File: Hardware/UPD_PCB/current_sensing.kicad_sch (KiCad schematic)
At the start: 48 parts, among them Q6 BSS84, U1 INA228, U2 INA228, U3 INA228, U4 INA228, U5 ACS711xEXLT-31AB

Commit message: Updated schematic
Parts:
- added TP5, TP6: TestPoint, TestPoint:TestPoint_Loop_D2.54mm_Drill1.5mm_Beaded, symbol Connector:TestPoint
- C23, C24, C27, C28: value C -> 100nF; footprint (none) -> Capacitor_SMD:C_0603_1608Metric_Pad1.08x0.95mm_HandSolder
- TP1, TP2, TP3, TP4: footprint (none) -> TestPoint:TestPoint_Loop_D2.54mm_Drill1.5mm_Beaded
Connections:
- net +5V: now also U2.1 (A1), U3.2 (A0), U4.1 (A1), U4.2 (A0)
- net GND: now also TP5.1, TP6.1; no longer U2.1 (A1), U3.2 (A0), U4.1 (A1), U4.2 (A0)

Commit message: Updated design
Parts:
- added C31: 0.1µF, symbol Device:C
- added C32: 100nF, Capacitor_SMD:C_0603_1608Metric_Pad1.08x0.95mm_HandSolder, symbol Device:C
- added R44: R_Shunt, symbol Device:R_Shunt
- added R45, R46: R50, Resistor_SMD:R_0603_1608Metric_Pad0.98x0.95mm_HandSolder, symbol Device:R
- added R47, R48, R49: 10k, Resistor_SMD:R_0603_1608Metric_Pad0.98x0.95mm_HandSolder, symbol Device:R
- added TP7: TestPoint, TestPoint:TestPoint_Loop_D2.54mm_Drill1.5mm_Beaded, symbol Connector:TestPoint
- added U6: INA228, Package_SO:VSSOP-10_3x3mm_P0.5mm, symbol Sensor_Energy:INA228
- C21, C22, C25, C26: value C -> 0.1µF
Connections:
- net +19V: no longer R24.1, TP4.1, U4.8 (Vbus)
- net +19V_out: no longer R24.4
- net +24V: no longer R12.1, TP2.1, U2.8 (Vbus)
- net +24V_out: no longer R12.4
- net +5V: now also R24.1, TP4.1, U4.8 (Vbus), C32.1, R47.2, R48.2, R49.2, U6.6 (VS)
- net GND: now also C32.2, U6.7 (GND)
- net INA_SCL: now also R48.1, U6.5 (SCL)
- net INA_SDA: now also R47.1, U6.1 (A1), U6.2 (A0), U6.4 (SDA)
- net INA_alert_19V: now also R49.1, U6.3 (~{Alert})
- new net: R44.2, R45.1
- new net: R44.3, R46.1
- new net: C31.1, R45.2, U6.10 (Vin+)
- new net: C31.2, R46.2, U6.9 (Vin-)
- new net +12V: R12.1, TP2.1, U2.8 (Vbus)
- new net +12V_out: R12.4
- new net +16V: R44.1, TP7.1, U6.8 (Vbus)
- new net +16V_out: R44.4
- new net +5V_out: R24.4
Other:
- moved on the sheet: C29, C30, D1, Q6, R31, R32, R33, R34, R35, R36, R37, U5

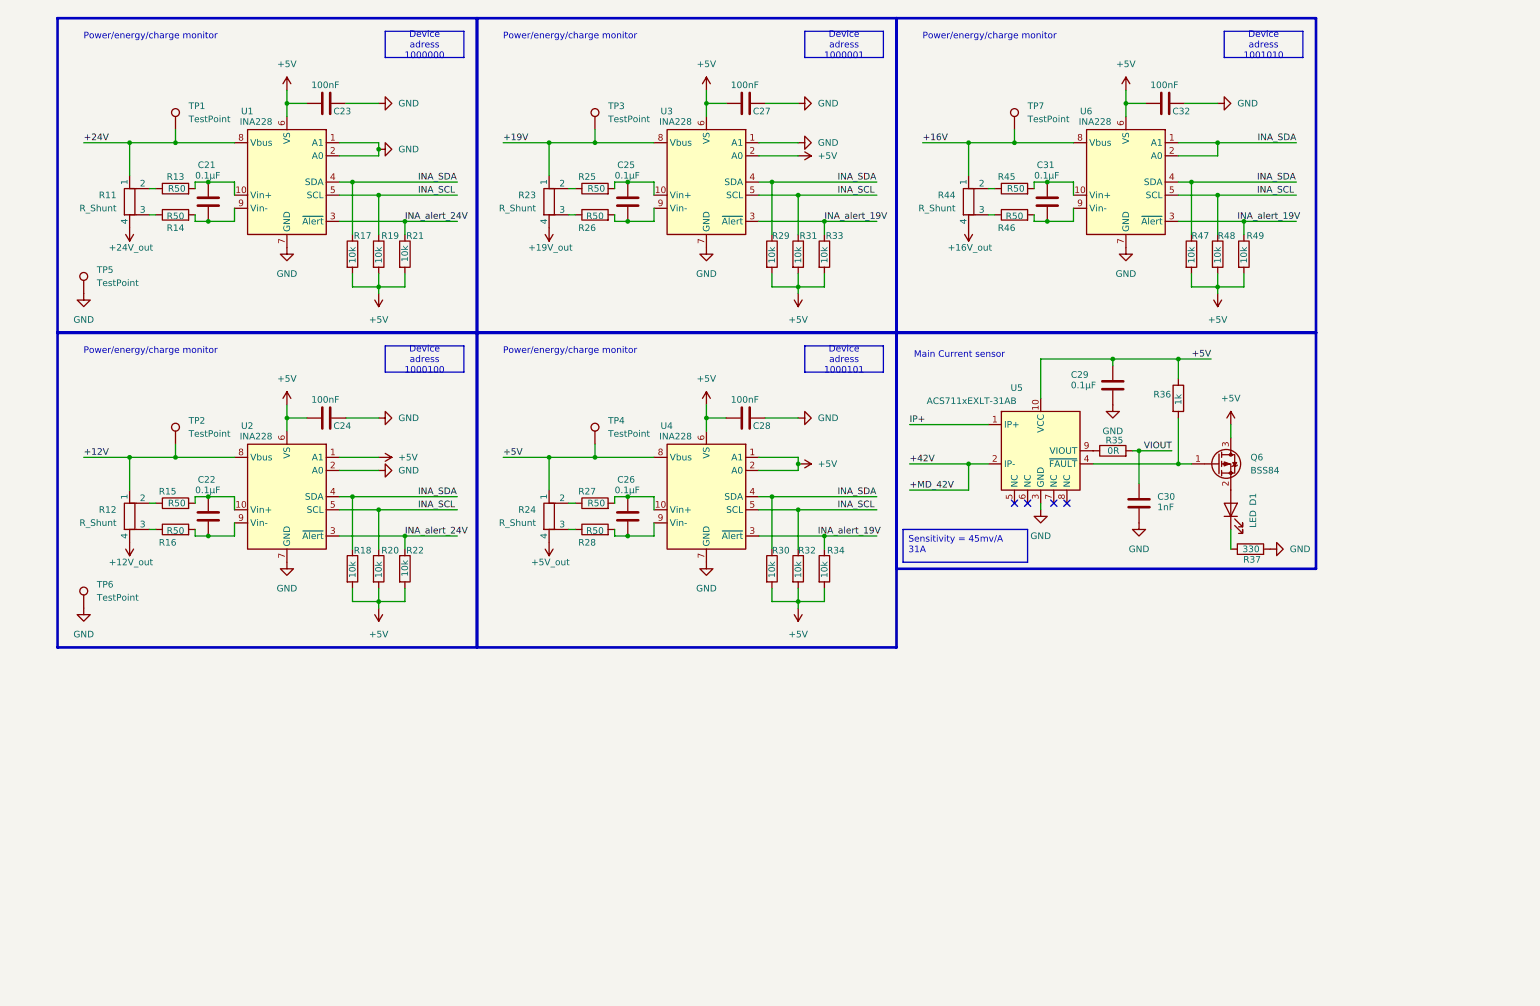
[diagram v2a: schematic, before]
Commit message: Updated schematic (before INA219 integration)
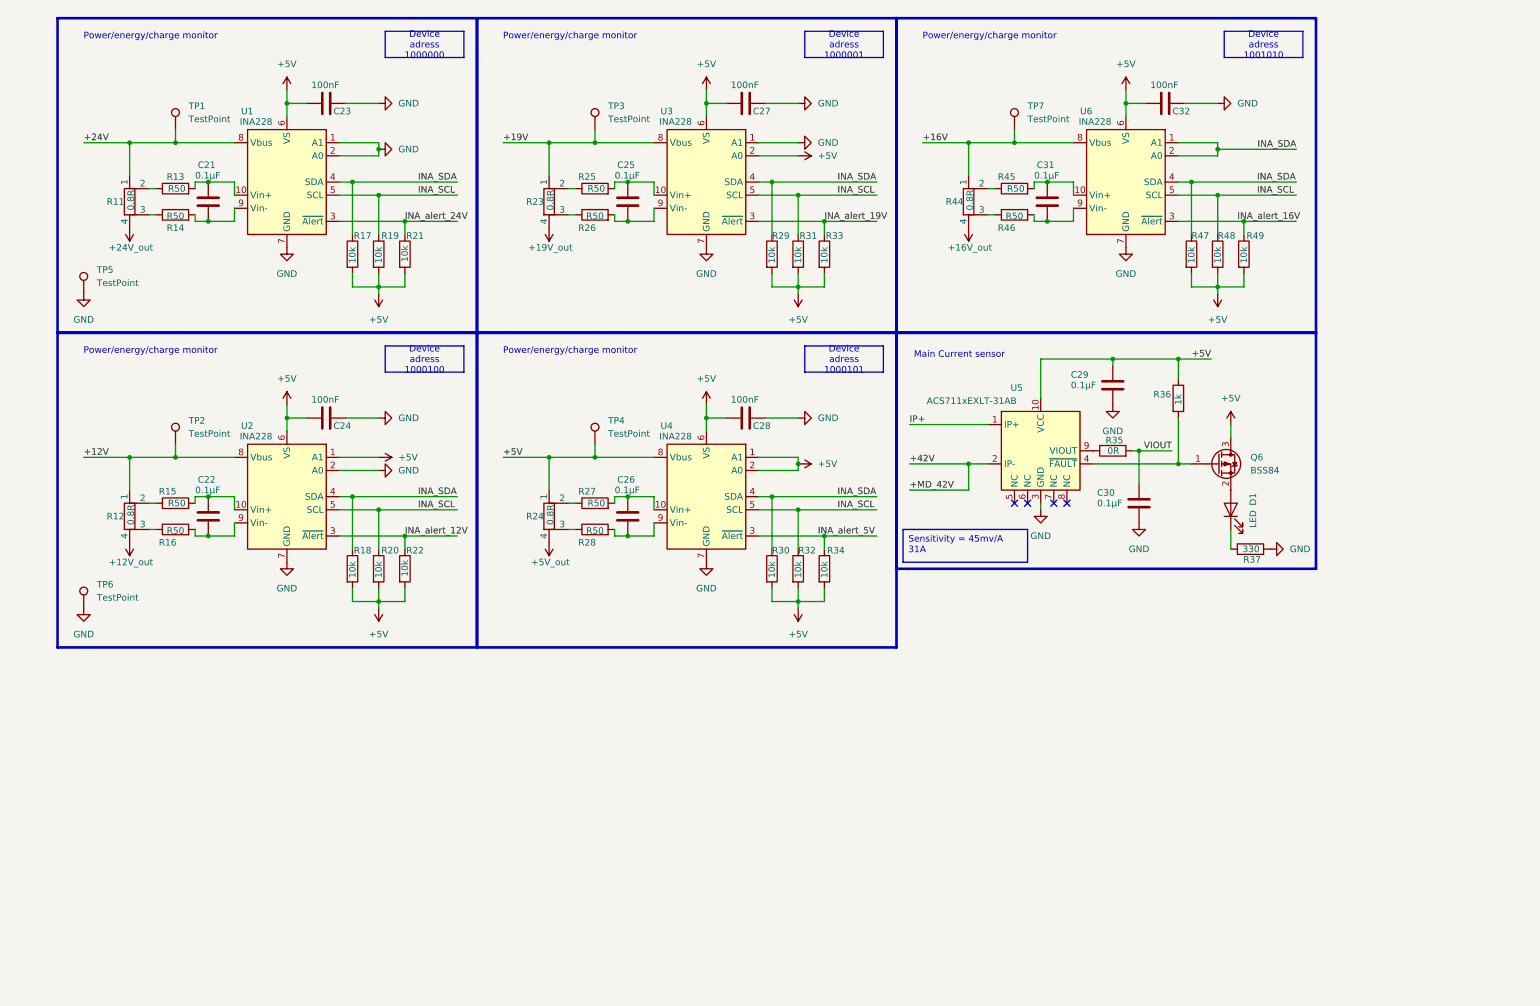
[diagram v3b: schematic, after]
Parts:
- C29: footprint (none) -> Capacitor_SMD:C_0603_1608Metric_Pad1.08x0.95mm_HandSolder
- C30: value 1nF -> 0.1µF; footprint (none) -> Capacitor_SMD:C_0603_1608Metric_Pad1.08x0.95mm_HandSolder
- D1: footprint (none) -> LED_SMD:LED_0603_1608Metric_Pad1.05x0.95mm_HandSolder
- R11, R12, R23, R24, R44: value R_Shunt -> 0.8R; footprint (none) -> Resistor_SMD:R_2512_6332Metric_Pad1.40x3.35mm_HandSolder
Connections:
- net INA_alert_19V: no longer R34.1, R49.1, U4.3 (~{Alert}), U6.3 (~{Alert})
- net INA_alert_24V: no longer R22.1, U2.3 (~{Alert})
- new net INA_alert_12V: R22.1, U2.3 (~{Alert})
- new net INA_alert_16V: R49.1, U6.3 (~{Alert})
- new net INA_alert_5V: R34.1, U4.3 (~{Alert})

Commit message: Finalized Schematic
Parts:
- removed C21, C22, C25, C26, C31: 0.1µF, symbol Device:C
- removed C23, C24, C27: 100nF, Capacitor_SMD:C_0603_1608Metric_Pad1.08x0.95mm_HandSolder, symbol Device:C
- removed R11, R12, R23, R24, R44: 0.8R, Resistor_SMD:R_2512_6332Metric_Pad1.40x3.35mm_HandSolder, symbol Device:R_Shunt
- removed R13, R14, R26, R27, R46: R50, Resistor_SMD:R_0603_1608Metric_Pad0.98x0.95mm_HandSolder, symbol Device:R
- removed R19, R20, R47, R48, R49: 10k, Resistor_SMD:R_0603_1608Metric_Pad0.98x0.95mm_HandSolder, symbol Device:R
- removed TP1, TP2: TestPoint, TestPoint:TestPoint_Loop_D2.54mm_Drill1.5mm_Beaded, symbol Connector:TestPoint
- removed U1, U2, U3, U4, U6: INA228, Package_SO:VSSOP-10_3x3mm_P0.5mm, symbol Sensor_Energy:INA228
- added C29, C33, C34, C35, C36, C37, C38, C39, C40, C41: 0.1µF, Capacitor_SMD:C_0603_1608Metric_Pad1.08x0.95mm_HandSolder, symbol Device:C
- added R13, R14, R26, R27, R36, R37: 0.2R, Resistor_SMD:R_Shunt_Vishay_WSK2512_6332Metric_T2.21mm, symbol Device:R_Shunt
- added R24, R35, R42, R43, R44: 10k, Resistor_SMD:R_0603_1608Metric_Pad0.98x0.95mm_HandSolder, symbol Device:R
- added R38, R39, R40, R41: R50, Resistor_SMD:R_0603_1608Metric_Pad0.98x0.95mm_HandSolder, symbol Device:R
- added TP5, TP6, TP8, TP9: TestPoint, TestPoint:TestPoint_Loop_D2.54mm_Drill1.5mm_Beaded, symbol Connector:TestPoint
- added U2, U3, U4, U5, U6, U7: INA219AxD, Package_SO:SOIC-8_3.9x4.9mm_P1.27mm, symbol Sensor_Energy:INA219AxD
- C28, C32: value 100nF -> 0.1µF
- R17, R18, R29, R30, R31: value 10k -> R50
- R25, R45: value R50 -> 10k
- renumbered C29 to C30, C30 to C31, Q6 to Q7, R35 to R19, R36 to R20, R37 to R23, TP5 to TP1, TP6 to TP2, U5 to U1
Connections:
- net INA_alert_12V is gone; now on net INA_SDA: R22.1
- net INA_alert_19V is gone; now on net INA_SDA: R33.1
- net INA_alert_24V is gone; now on net INA_SDA: R21.1
- net INA_alert_5V is gone; now on net INA_SCL: R34.1
- net +16V: now also R37.1, TP9.1; no longer TP7.1
- net +16V_out: now also R37.4
- net +19V: now also R26.1, TP6.1; no longer TP3.1
- net +19V_out: now also R26.4
- net +24V: now also TP3.1, R13.1
- net +24V_out: now also R13.4
- net +5V: now also C32.2, R25.2, R45.2, C33.2, C36.2, C37.2, C40.2, C41.2, R24.2, R35.2, R36.4, R42.2, R43.2, R44.2, U2.5 (VS), U3.1 (A1), U3.5 (VS), U4.2 (A0), U4.5 (VS), U5.5 (VS), U6.1 (A1), U6.2 (A0), U6.5 (VS), U7.5 (VS); no longer C28.1, C32.1, R17.2, R18.2, R29.2, R30.2, R31.2, TP4.1
- net GND: now also C32.1, C33.1, C36.1, C37.1, C40.1, C41.1, TP5.1, U2.1 (A1), U2.2 (A0), U2.6 (GND), U3.2 (A0), U3.6 (GND), U4.1 (A1), U4.6 (GND), U5.6 (GND), U6.6 (GND), U7.6 (GND); no longer C28.2, C32.2
- net INA_SCL: now also R25.1, R45.1, R24.1, R35.1, R44.1, U2.4 (SCL), U3.4 (SCL), U4.4 (SCL), U5.1 (A1), U5.2 (A0), U5.4 (SCL), U6.4 (SCL), U7.4 (SCL); no longer R31.1, R32.1
- net INA_SDA: now also R32.1, R42.1, R43.1, U2.3 (SDA), U3.3 (SDA), U4.3 (SDA), U5.3 (SDA), U6.3 (SDA), U7.1 (A1), U7.2 (A0), U7.3 (SDA); no longer R17.1, R18.1, R29.1, R30.1
- net at R28.1: now also R26.2
- net at R28.2: now also C34.1, U4.8 (IN+)
- net at R15.1: now also R13.2
- net at R15.2: now also C28.1, U2.8 (IN+)
- net at R16.2: now also C28.2, U2.7 (IN-)
- net at R16.1: now also R13.3
- new net: C39.1, R40.2, U7.8 (IN+)
- new net: C39.2, R41.2, U7.7 (IN-)
- new net: C38.2, R39.2, U6.7 (IN-)
- new net: C38.1, R38.2, U6.8 (IN+)
- new net: R27.2, R30.1
- new net: R27.3, R31.1
- new net: R26.3, R29.1
- new net: C34.2, R29.2, U4.7 (IN-)
- new net: C35.1, R30.2, U5.8 (IN+)
- new net: R36.2, R38.1
- new net: R37.3, R41.1
- new net: C35.2, R31.2, U5.7 (IN-)
- new net: R37.2, R40.1
- new net: R14.2, R17.1
- new net: R14.3, R18.1
- new net: C29.1, R17.2, U3.8 (IN+)
- new net: R36.3, R39.1
- new net: C29.2, R18.2, U3.7 (IN-)
- new net +12V_1: R14.1, TP4.1
- new net +12V_1_out: R14.4
- new net +12V_2: R27.1, TP7.1
- new net +12V_2_out: R27.4
- new net +5V_NS: R36.1, TP8.1
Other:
- moved on the sheet: C30, C31, D1, Q7, R19, R20, R23, TP1, TP2, U1

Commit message: First board layout
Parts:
- R13, R14, R26, R27, R36, R37: footprint Resistor_SMD:R_Shunt_Vishay_WSK2512_6332Metric_T2.21mm -> Library:R_shunt_different_pad_layout
- TP1, TP2, TP3, TP4, TP5, TP6, TP7, TP8, TP9: footprint TestPoint:TestPoint_Loop_D2.54mm_Drill1.5mm_Beaded -> TestPoint:TestPoint_THTPad_D1.0mm_Drill0.5mm

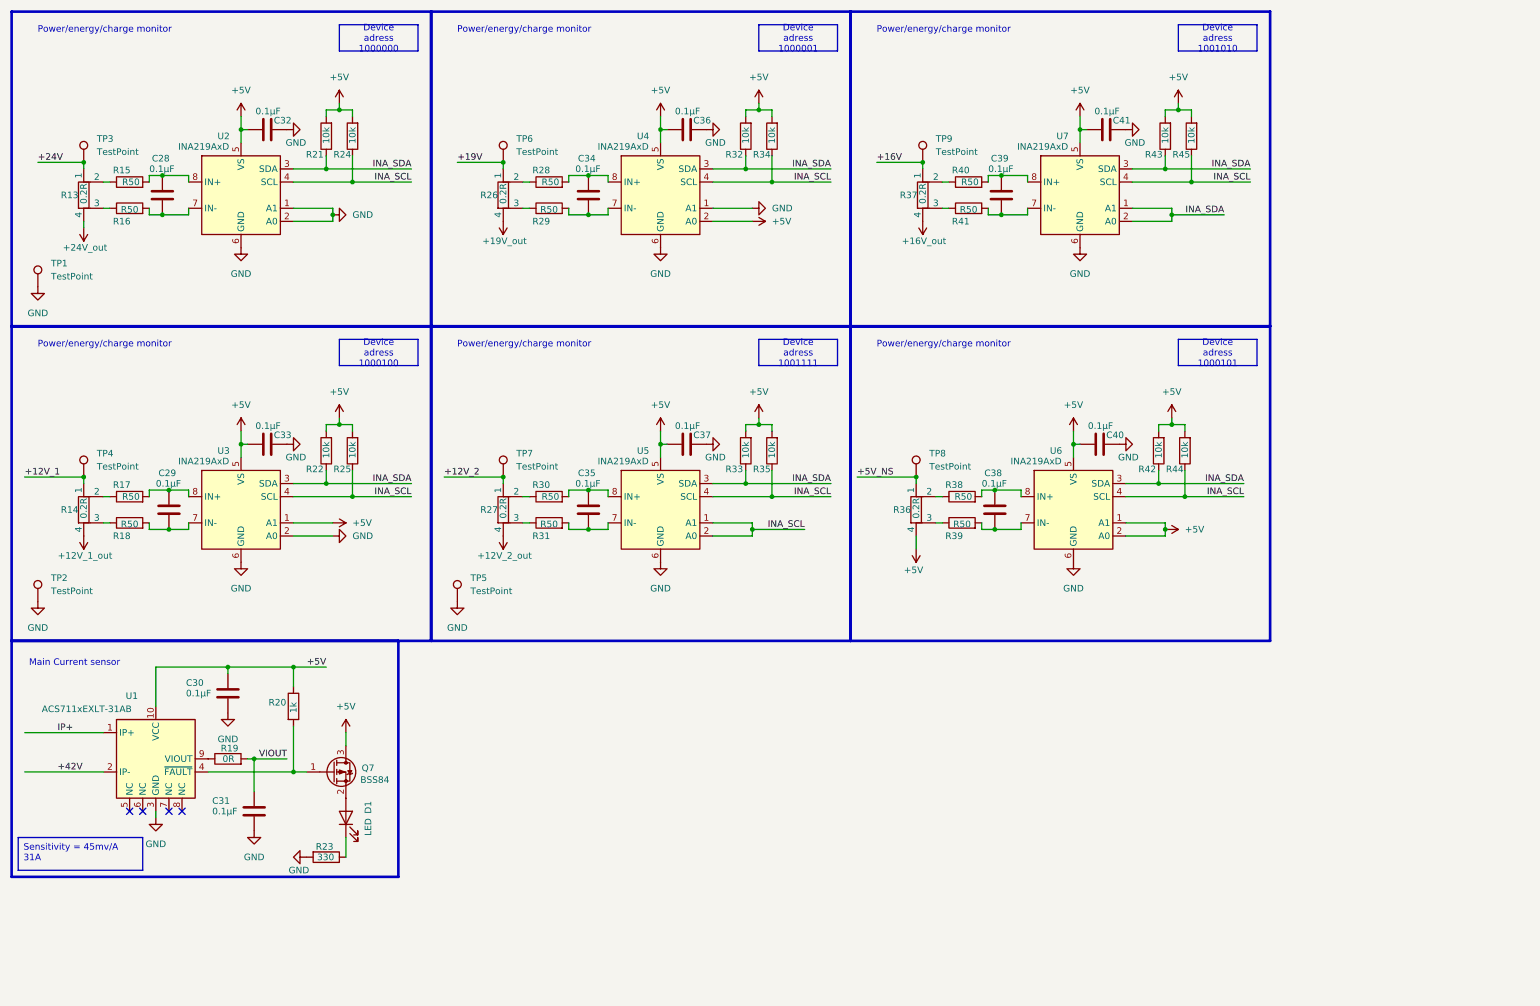
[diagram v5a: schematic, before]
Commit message: Pcb layout before changing inductor
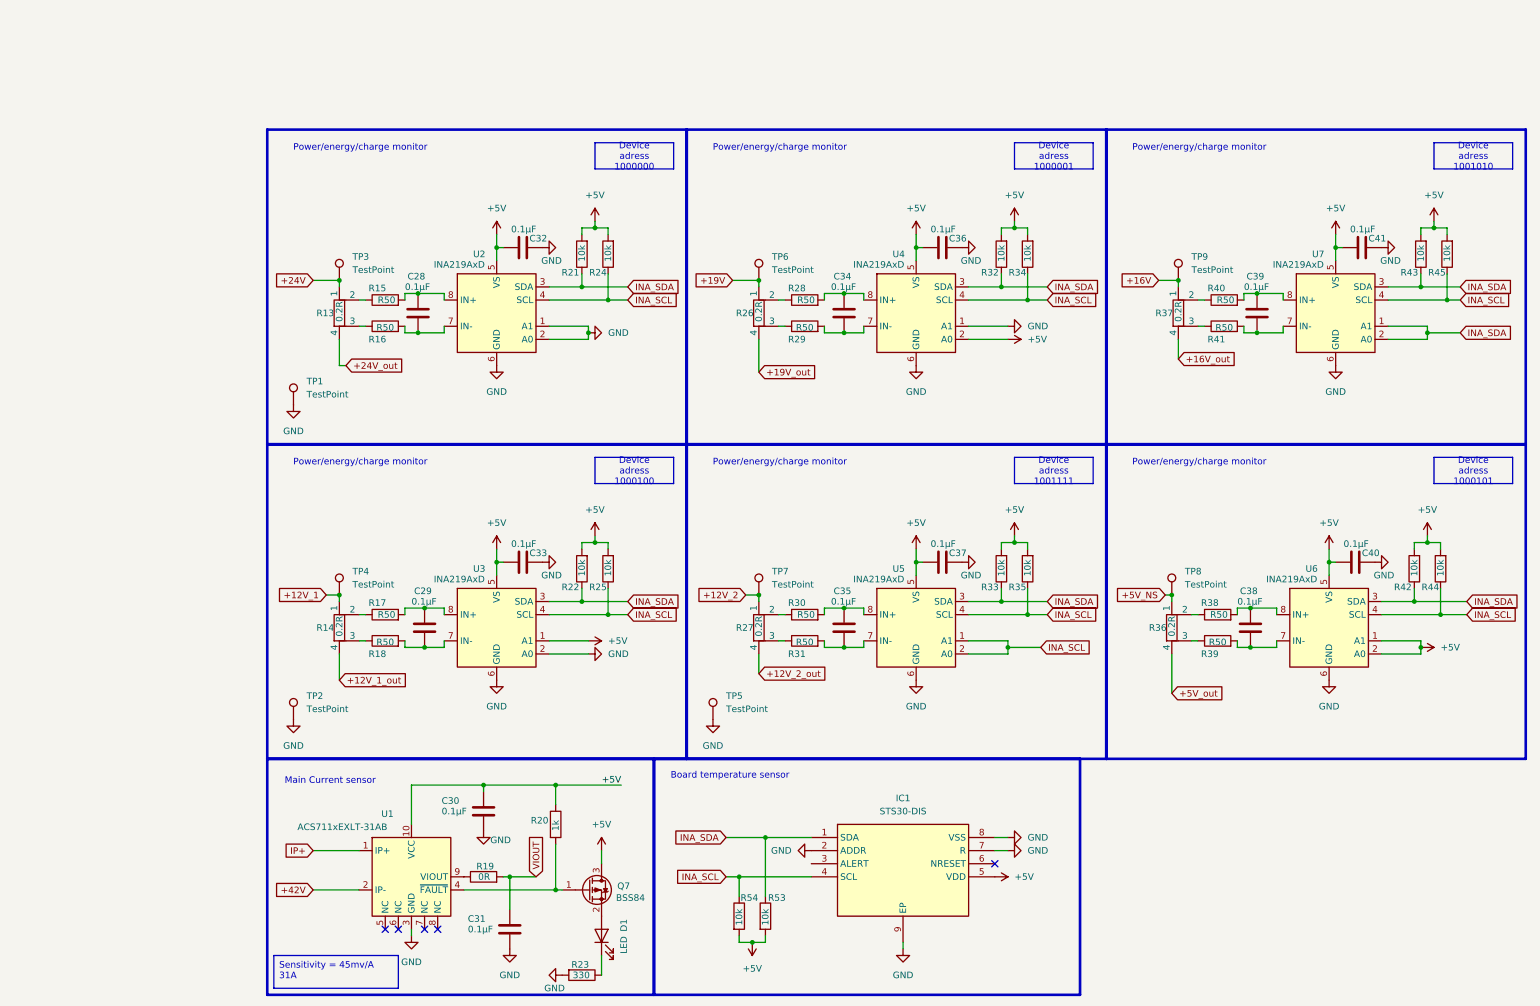
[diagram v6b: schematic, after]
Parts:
- added IC1: STS30-DIS, SON50P250X250X100-9N-D, symbol STS30-DIS:STS30-DIS
- added R53, R54: 10k, Resistor_SMD:R_0603_1608Metric_Pad0.98x0.95mm_HandSolder, symbol Device:R
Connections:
- net +5V: now also IC1.5 (VDD), R53.2, R54.2; no longer R36.4
- net GND: now also IC1.2 (ADDR), IC1.7 (R), IC1.8 (VSS), IC1.9 (EP)
- net INA_SCL: now also IC1.4 (SCL), R54.1
- net INA_SDA: now also IC1.1 (SDA), R53.1
- new net +5V_out: R36.4
- no-connect marks 4 -> 5
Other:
- note added: "Board temperature sensor"
- moved on the sheet: C28, C29, C30, C31, C32, C33, C34, C35, C36, C37, C38, C39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
